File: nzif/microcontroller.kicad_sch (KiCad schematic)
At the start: 25 parts, among them J112 Conn_01x02, U157 W25Q128JVS, U158 MCP23017_SO, U159 RP2040

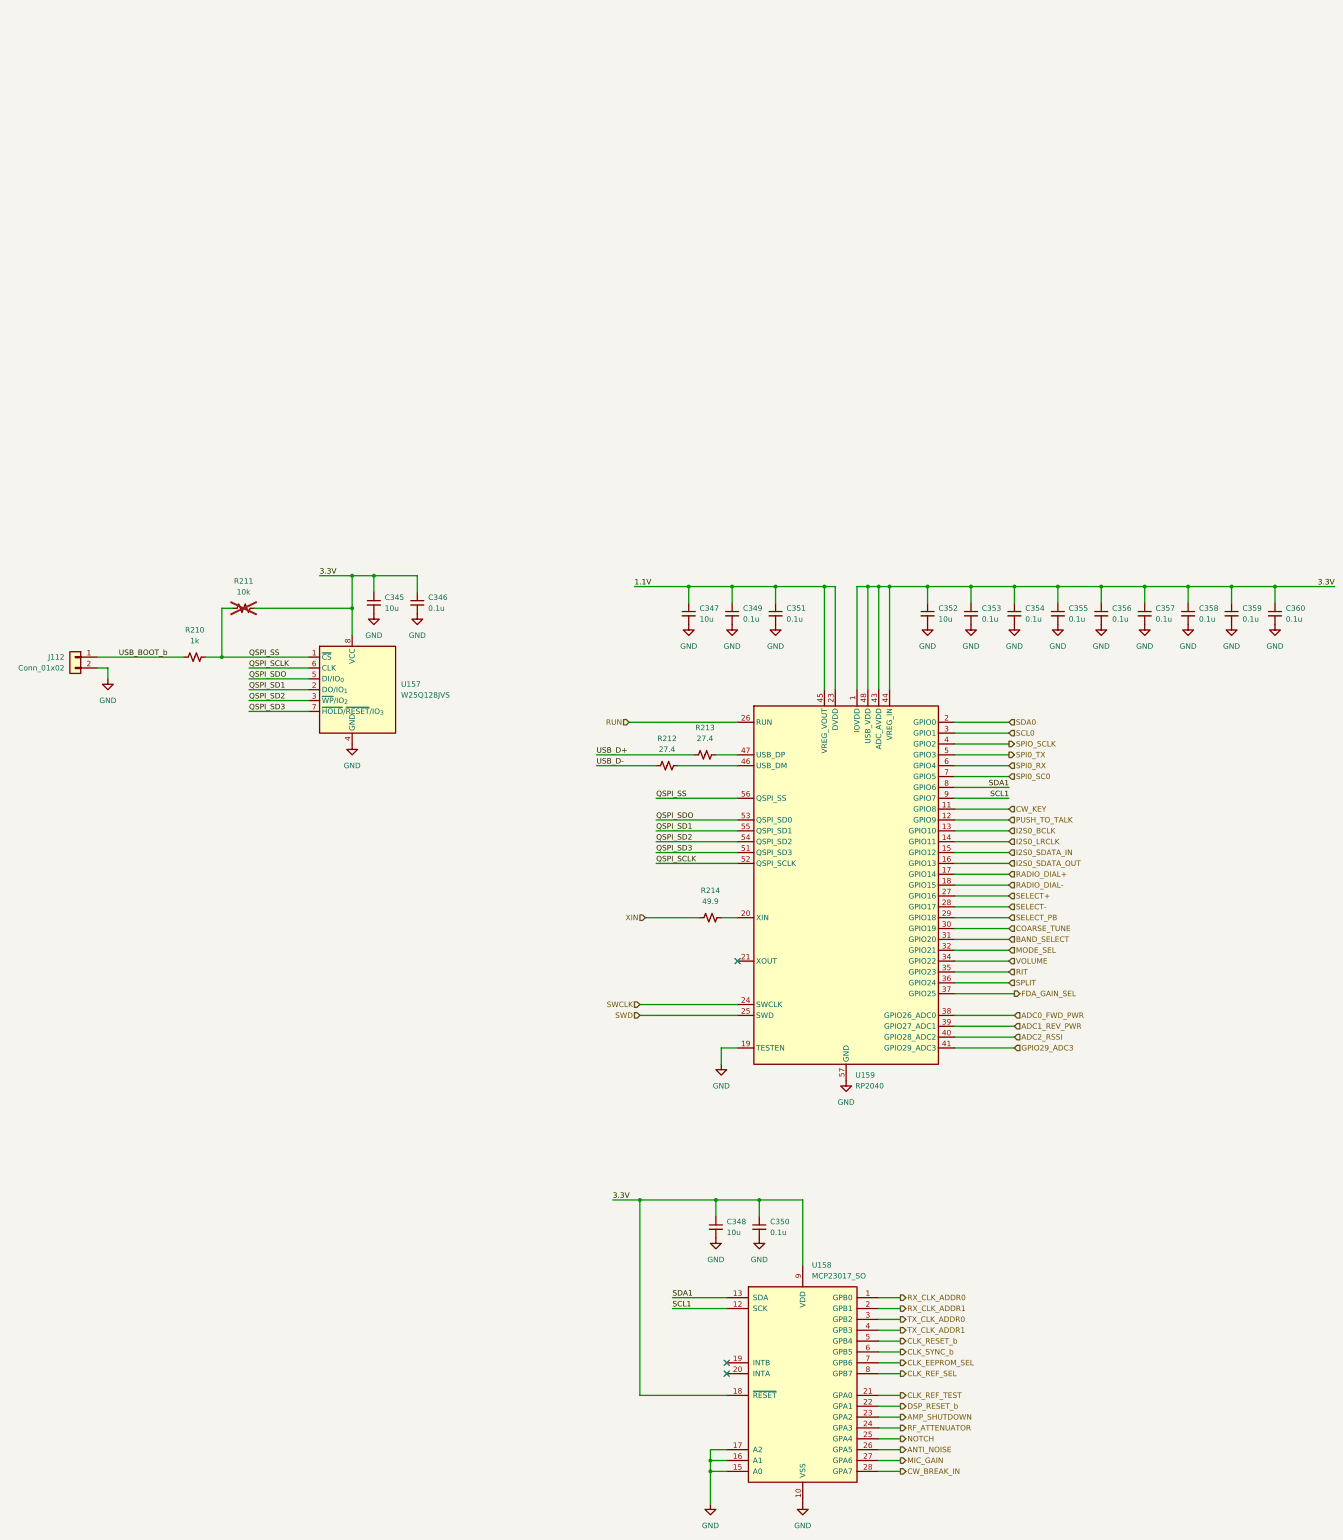
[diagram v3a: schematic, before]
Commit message: updated power on all schematics
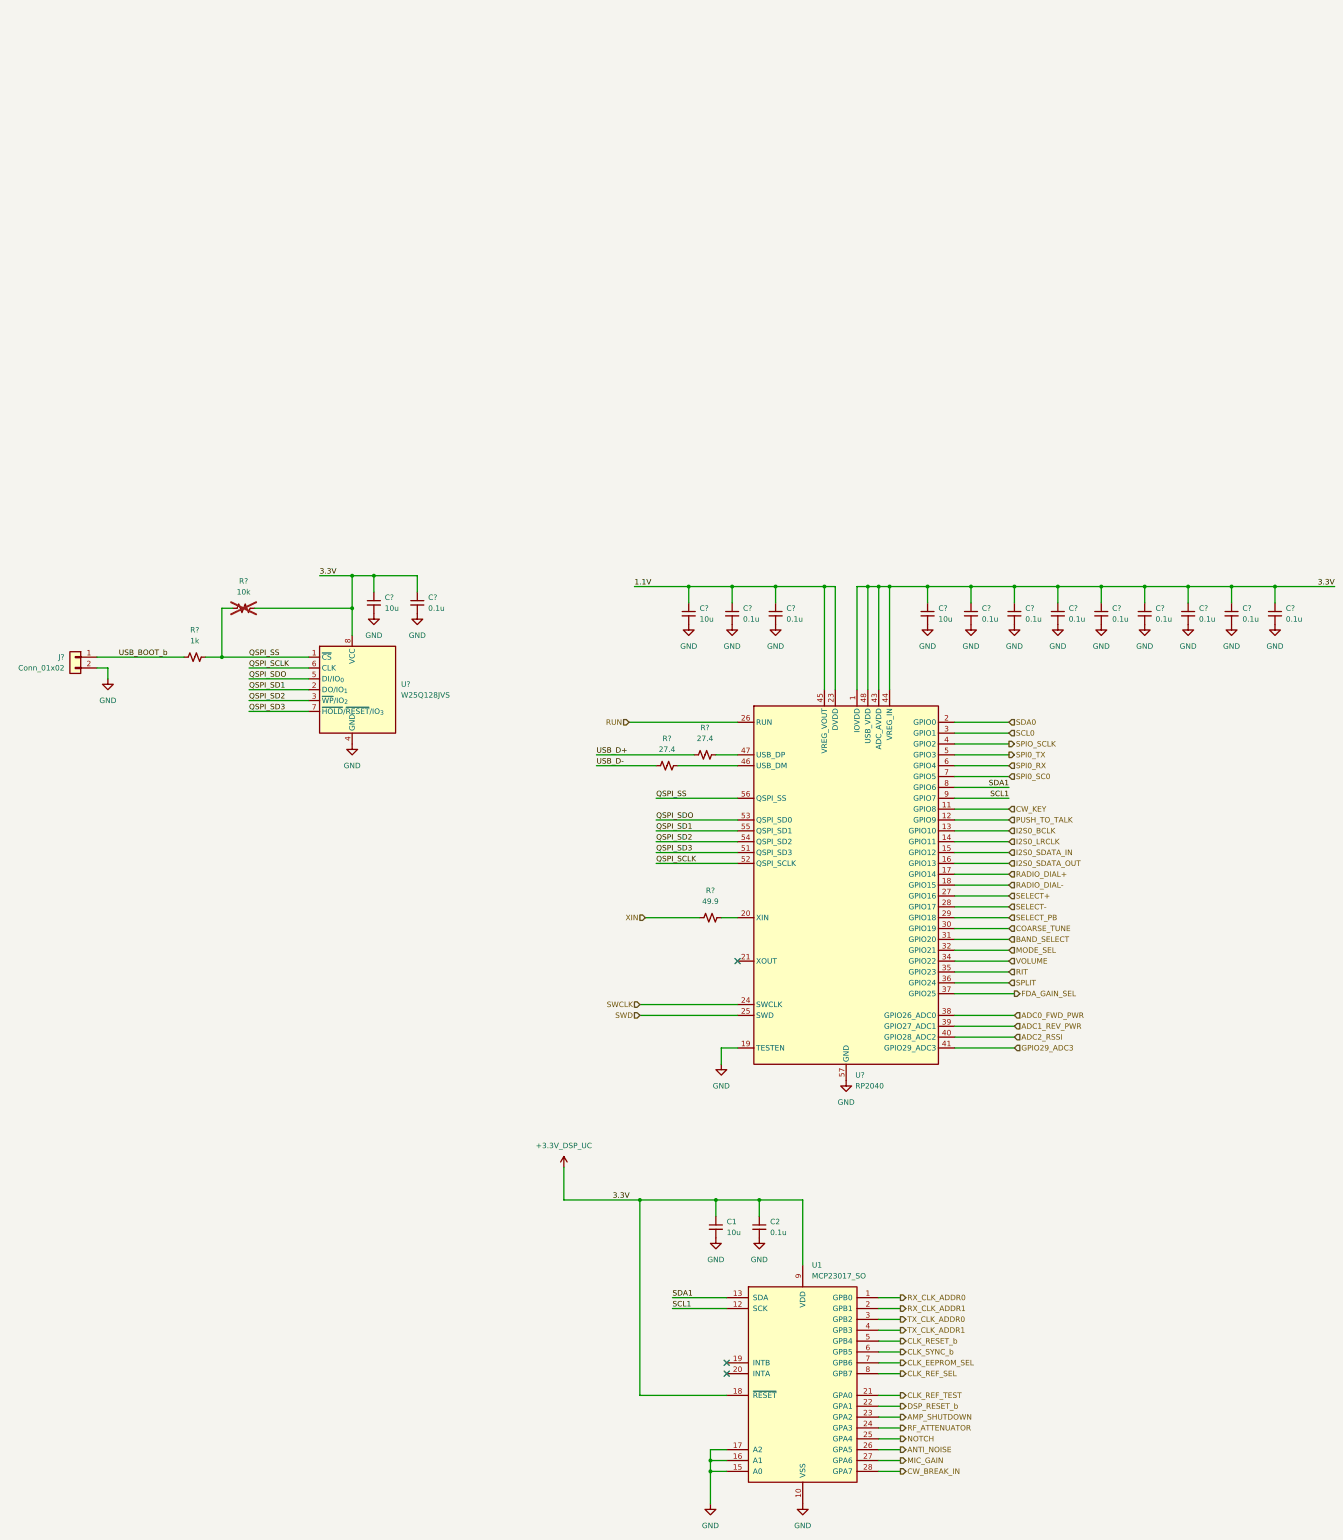
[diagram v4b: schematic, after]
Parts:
- renumbered C348 to C1, C350 to C2, C345 to C?, C351 to C?, C357 to C?, C358 to C?, C346 to C?, C360 to C?, C354 to C?, C356 to C?, C353 to C?, C349 to C?, C347 to C?, C352 to C?, C359 to C?, C355 to C?, J112 to J?, R211 to R?, R213 to R?, R214 to R?, R210 to R?, R212 to R?, U158 to U1, U157 to U?, U159 to U?
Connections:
- net 3.3V renamed +3.3V_DSP_UC
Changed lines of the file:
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@@
 	(wire
 		(pts
+			(xy 160.02 166.37) (xy 160.02 173.99)
+		)
+		(stroke
+			(width 0)
+			(type default)
+		)
+	)
+	(wire
+		(pts
 			(xy 255.27 30.48) (xy 245.11 30.48)
 		)
@@
 	(wire
 		(pts
-			(xy 171.45 173.99) (xy 177.8 173.99)
+			(xy 181.61 80.01) (xy 200.66 80.01)
 		)
 		(stroke
@@
 	(wire
 		(pts
-			(xy 181.61 80.01) (xy 200.66 80.01)
+			(xy 181.61 92.71) (xy 200.66 92.71)
 		)
 		(stroke
@@
 	(wire
 		(pts
-			(xy 181.61 92.71) (xy 200.66 92.71)
+			(xy 160.02 173.99) (xy 177.8 173.99)
 		)
 		(stroke
@@
 		(dnp no)
 		(fields_autoplaced yes)
-		(property "Reference" "C345"
+		(property "Reference" "C?"
 			(at 118.11 33.0262 0)
 			(effects
@@
 		(dnp yes)
 		(fields_autoplaced yes)
-		(property "Reference" "R211"
+		(property "Reference" "R?"
 			(at 85.09 29.21 90)
 			(effects
@@
 		(dnp no)
 		(fields_autoplaced yes)
-		(property "Reference" "R213"
+		(property "Reference" "R?"
 			(at 193.04 63.5 90)
 			(effects
@@
 		(dnp no)
 		(fields_autoplaced yes)
-		(property "Reference" "#PWR0385"
+		(property "Reference" "#PWR?"
 			(at 189.23 45.72 0)
 			(effects
@@
 		(dnp no)
 		(fields_autoplaced yes)
-		(property "Reference" "C351"
+		(property "Reference" "C?"
 			(at 212.09 35.5662 0)
 			(effects
@@
 		(dnp no)
 		(fields_autoplaced yes)
-		(property "Reference" "#PWR0393"
+		(property "Reference" "#PWR?"
 			(at 226.06 152.4 0)
 			(effects
@@
 		(dnp no)
 		(fields_autoplaced yes)
-		(property "Reference" "#PWR0391"
+		(property "Reference" "#PWR?"
 			(at 209.55 45.72 0)
 			(effects
@@
 		(dnp no)
 		(fields_autoplaced yes)
-		(property "Reference" "C357"
+		(property "Reference" "C?"
 			(at 298.45 35.5662 0)
 			(effects
@@
 		(dnp no)
 		(fields_autoplaced yes)
-		(property "Reference" "#PWR0387"
+		(property "Reference" "#PWR01"
 			(at 195.58 189.23 0)
 			(effects
@@
 		(dnp no)
 		(fields_autoplaced yes)
-		(property "Reference" "#PWR0395"
+		(property "Reference" "#PWR?"
 			(at 255.27 45.72 0)
 			(effects
@@
 		(dnp no)
 		(fields_autoplaced yes)
-		(property "Reference" "C358"
+		(property "Reference" "C?"
 			(at 308.61 35.5662 0)
 			(effects
@@
 		(dnp no)
 		(fields_autoplaced yes)
-		(property "Reference" "C346"
+		(property "Reference" "C?"
 			(at 128.27 33.0262 0)
 			(effects
@@
 		(dnp no)
 		(fields_autoplaced yes)
-		(property "Reference" "R214"
+		(property "Reference" "R?"
 			(at 194.31 101.6 90)
 			(effects
@@
 		(dnp no)
 		(fields_autoplaced yes)
-		(property "Reference" "#PWR0396"
+		(property "Reference" "#PWR?"
 			(at 265.43 45.72 0)
 			(effects
@@
 		(dnp no)
 		(fields_autoplaced yes)
-		(property "Reference" "R210"
+		(property "Reference" "R?"
 			(at 73.66 40.64 90)
 			(effects
@@
 		(dnp no)
 		(fields_autoplaced yes)
-		(property "Reference" "#PWR0392"
+		(property "Reference" "#PWR?"
 			(at 215.9 251.46 0)
 			(effects
@@
 		(dnp no)
 		(fields_autoplaced yes)
-		(property "Reference" "C360"
+		(property "Reference" "C?"
 			(at 328.93 35.5662 0)
 			(effects
@@
 		(dnp no)
 		(fields_autoplaced yes)
-		(property "Reference" "C354"
+		(property "Reference" "C?"
 			(at 267.97 35.5662 0)
 			(effects
@@
 		(dnp no)
 		(fields_autoplaced yes)
-		(property "Reference" "R212"
+		(property "Reference" "R?"
 			(at 184.15 66.04 90)
 			(effects
@@
 	)
 	(symbol
+		(lib_id "power:+3.3V")
+		(at 160.02 166.37 0)
+		(unit 1)
+		(exclude_from_sim no)
+		(in_bom yes)
+		(on_board yes)
+		(dnp no)
+		(fields_autoplaced yes)
+		(property "Reference" "#PWR04"
+			(at 160.02 170.18 0)
+			(effects
+				(font
+					(size 1.27 1.27)
+				)
+				(hide yes)
+			)
+		)
+		(property "Value" "+3.3V_DSP_UC"
+			(at 160.02 161.29 0)
+			(effects
+				(font
+					(size 1.27 1.27)
+				)
+			)
+		)
+		(property "Footprint" ""
+			(at 160.02 166.37 0)
+			(effects
+				(font
+					(size 1.27 1.27)
+				)
+				(hide yes)
+			)
+		)
+		(property "Datasheet" ""
+			(at 160.02 166.37 0)
+			(effects
+				(font
+					(size 1.27 1.27)
+				)
+				(hide yes)
+			)
+		)
+		(property "Description" "Power symbol creates a global label with name \"+3.3V\""
+			(at 160.02 166.37 0)
+			(effects
+				(font
+					(size 1.27 1.27)
+				)
+				(hide yes)
+			)
+		)
+		(pin "1"
+		)
+		(instances
+			(project ""
+				(path "/71d46858-c1d3-4044-8b5a-4338b45f747c"
+					(reference "#PWR04")
+					(unit 1)
+				)
+			)
+		)
+	)
+	(symbol
 		(lib_id "power:GND")
 		(at 275.59 39.37 0)
@@
 		(dnp no)
 		(fields_autoplaced yes)
-		(property "Reference" "#PWR0397"
+		(property "Reference" "#PWR?"
 			(at 275.59 45.72 0)
 			(effects
@@
 		(dnp no)
 		(fields_autoplaced yes)
-		(property "Reference" "C356"
+		(property "Reference" "C?"
 			(at 288.29 35.5662 0)
 			(effects
@@
 		(dnp no)
 		(fields_autoplaced yes)
-		(property "Reference" "#PWR0402"
+		(property "Reference" "#PWR?"
 			(at 326.39 45.72 0)
 			(effects
@@
 		(dnp no)
 		(fields_autoplaced yes)
-		(property "Reference" "U157"
+		(property "Reference" "U?"
 			(at 121.92 53.3399 0)
 			(effects
@@
 		(dnp no)
 		(fields_autoplaced yes)
-		(property "Reference" "J112"
+		(property "Reference" "J?"
 			(at 43.18 46.9899 0)
 			(effects
@@
 		(dnp no)
 		(fields_autoplaced yes)
-		(property "Reference" "C350"
+		(property "Reference" "C2"
 			(at 208.28 179.0762 0)
 			(effects
@@
 		(dnp no)
 		(fields_autoplaced yes)
-		(property "Reference" "C353"
+		(property "Reference" "C?"
 			(at 257.81 35.5662 0)
 			(effects
@@
 		(dnp no)
 		(fields_autoplaced yes)
-		(property "Reference" "#PWR0381"
+		(property "Reference" "#PWR?"
 			(at 53.34 58.42 0)
 			(effects
@@
 		(dnp no)
 		(fields_autoplaced yes)
-		(property "Reference" "#PWR0390"
+		(property "Reference" "#PWR02"
 			(at 205.74 189.23 0)
 			(effects
@@
 		(dnp no)
 		(fields_autoplaced yes)
-		(property "Reference" "#PWR0388"
+		(property "Reference" "#PWR?"
 			(at 196.85 148.59 0)
 			(effects
@@
 		(dnp no)
 		(fields_autoplaced yes)
-		(property "Reference" "#PWR0400"
+		(property "Reference" "#PWR?"
 			(at 306.07 45.72 0)
 			(effects
@@
 		(dnp no)
 		(fields_autoplaced yes)
-		(property "Reference" "C349"
+		(property "Reference" "C?"
 			(at 201.93 35.5662 0)
 			(effects
@@
 		(dnp no)
 		(fields_autoplaced yes)
-		(property "Reference" "#PWR0398"
+		(property "Reference" "#PWR?"
 			(at 285.75 45.72 0)
 			(effects
@@
 		(dnp no)
 		(fields_autoplaced yes)
-		(property "Reference" "#PWR0383"
+		(property "Reference" "#PWR?"
 			(at 115.57 43.18 0)
 			(effects
@@
 		(dnp no)
 		(fields_autoplaced yes)
-		(property "Reference" "C347"
+		(property "Reference" "C?"
 			(at 191.77 35.5662 0)
 			(effects
@@
 		(dnp no)
 		(fields_autoplaced yes)
-		(property "Reference" "C352"
+		(property "Reference" "C?"
 			(at 247.65 35.5662 0)
 			(effects
@@
 		(dnp no)
 		(fields_autoplaced yes)
-		(property "Reference" "#PWR0384"
+		(property "Reference" "#PWR?"
 			(at 125.73 43.18 0)
 			(effects
@@
 		(dnp no)
 		(fields_autoplaced yes)
-		(property "Reference" "U158"
+		(property "Reference" "U1"
 			(at 218.0433 189.23 0)
 			(effects
@@
 		(dnp no)
 		(fields_autoplaced yes)
-		(property "Reference" "#PWR0394"
+		(property "Reference" "#PWR?"
 			(at 245.11 45.72 0)
 			(effects
@@
 		(dnp no)
 		(fields_autoplaced yes)
-		(property "Reference" "U159"
+		(property "Reference" "U?"
 			(at 228.2033 144.78 0)
 			(effects
@@
 		(dnp no)
 		(fields_autoplaced yes)
-		(property "Reference" "#PWR0389"
+		(property "Reference" "#PWR?"
 			(at 199.39 45.72 0)
 			(effects
@@
 		(dnp no)
 		(fields_autoplaced yes)
-		(property "Reference" "C359"
+		(property "Reference" "C?"
 			(at 318.77 35.5662 0)
 			(effects
@@
 		(dnp no)
 		(fields_autoplaced yes)
-		(property "Reference" "#PWR0382"
+		(property "Reference" "#PWR?"
 			(at 110.49 73.66 0)
 			(effects
@@
 		(dnp no)
 		(fields_autoplaced yes)
-		(property "Reference" "#PWR0399"
+		(property "Reference" "#PWR?"
 			(at 295.91 45.72 0)
 			(effects
@@
 		(dnp no)
 		(fields_autoplaced yes)
-		(property "Reference" "C355"
+		(property "Reference" "C?"
 			(at 278.13 35.5662 0)
 			(effects
@@
 		(dnp no)
 		(fields_autoplaced yes)
-		(property "Reference" "C348"
+		(property "Reference" "C1"
 			(at 198.12 179.0762 0)
 			(effects
@@
 		(dnp no)
 		(fields_autoplaced yes)
-		(property "Reference" "#PWR0386"
+		(property "Reference" "#PWR03"
 			(at 194.31 251.46 0)
 			(effects
@@
 		(dnp no)
 		(fields_autoplaced yes)
-		(property "Reference" "#PWR0401"
+		(property "Reference" "#PWR?"
 			(at 316.23 45.72 0)
 			(effects
